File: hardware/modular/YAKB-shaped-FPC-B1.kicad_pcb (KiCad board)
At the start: 2 copper layers, 223 x 99.3 mm, 2 parts

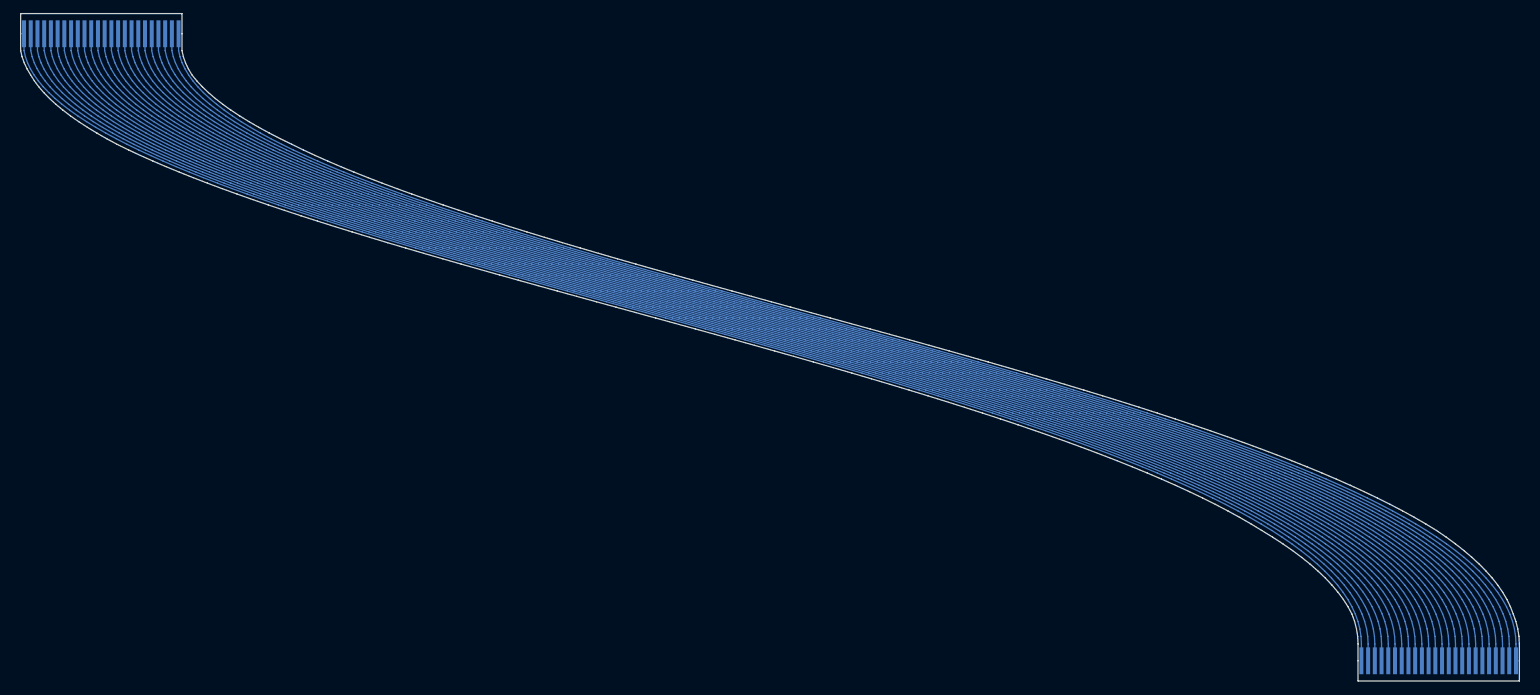
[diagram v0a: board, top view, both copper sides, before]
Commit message: fix(hardware): correct FPC mating geometry and add fit coupons
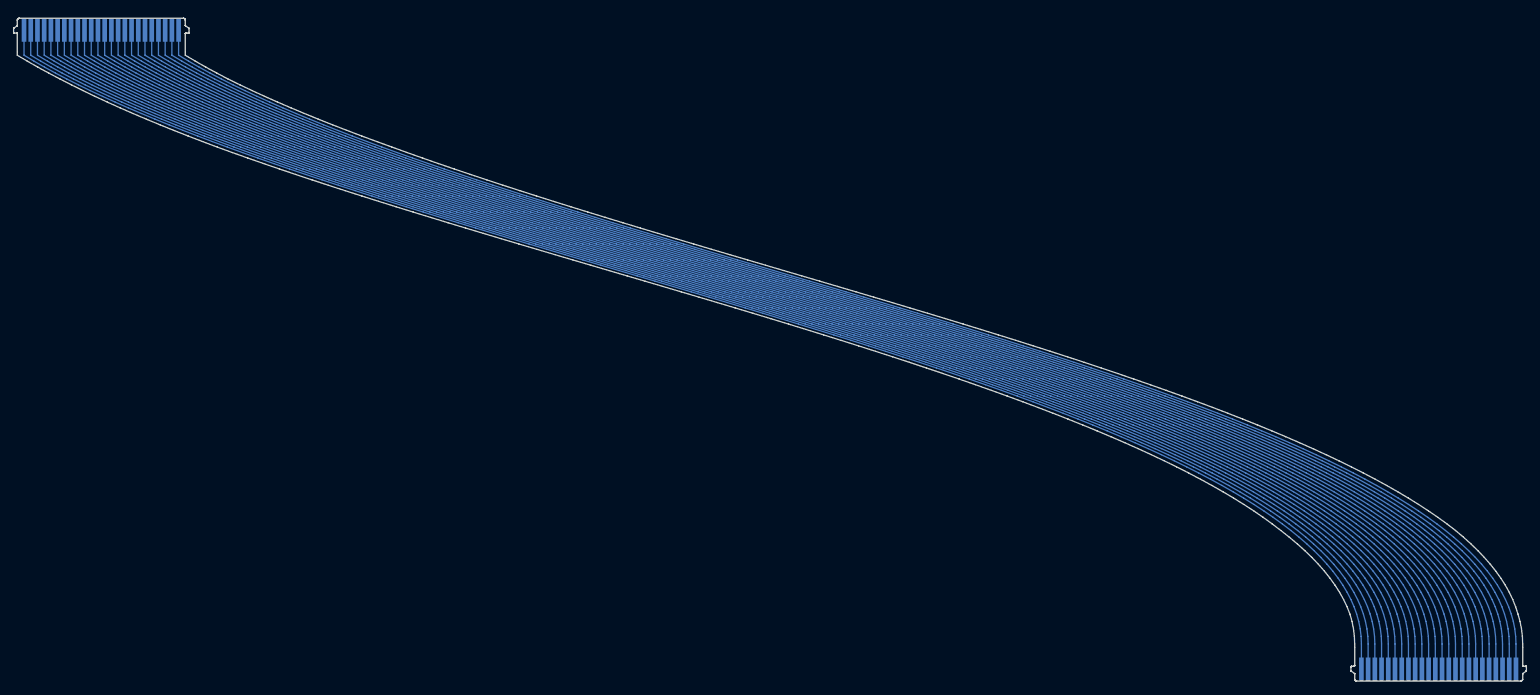
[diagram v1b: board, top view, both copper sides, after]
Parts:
- J_A, J_B: value FPC_BOTTOM_CONTACT_1mm -> MOLEX_200528_1mm_BOTTOM
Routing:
- net LINE17_GND: track 229.0 -> 230.1 mm
- net LINE08_ROW_DRV4: track 229.0 -> 230.1 mm
- net LINE09_GND: track 229.0 -> 230.1 mm
- net LINE12_MUX_C: track 229.0 -> 230.1 mm
- net LINE06_ROW_DRV2: track 229.0 -> 230.1 mm
- net LINE01_GND: track 229.0 -> 230.1 mm
- net LINE24_GND: track 229.0 -> 230.1 mm
- net LINE23_BAT_SW: track 229.0 -> 230.1 mm
- net LINE21_GND: track 229.0 -> 230.1 mm
- net LINE03_GND: track 229.0 -> 230.1 mm
- net LINE02_VCC: track 229.0 -> 230.1 mm
- net LINE16_AFE_ON_N: track 229.0 -> 230.1 mm
- net LINE14_MUX1_INH: track 229.0 -> 230.1 mm
- net LINE11_MUX_B: track 229.0 -> 230.1 mm
- net LINE10_MUX_A: track 229.0 -> 230.1 mm
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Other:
- board size 223 x 99.3 mm -> 225.1 x 98.6 mm
